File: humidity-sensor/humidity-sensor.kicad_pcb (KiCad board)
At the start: 2 copper layers, 17.8 x 142.4 mm, 9 parts, among them J1 AVR-ISP-6, J2 i2c, U1 ATtiny45-20SU

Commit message: peak-detect: add mixers humidity-sensor: fix bugs, smaller PCB
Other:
- board text added: "capacitive humidity sensor v2 lars@ibp.de"
- board text removed: "capacitive humidity sensor v1 lars@ibp.de"
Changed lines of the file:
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@@
     (effects (font (size 1 1) (thickness 0.15)))
   )
-  (gr_text "capacitive humidity \nsensor v1\nlars@ibp.de" (at 120.65 55.88) (layer F.SilkS)
+  (gr_text "capacitive humidity \nsensor v2\nlars@ibp.de" (at 120.65 55.88) (layer F.SilkS)
     (effects (font (size 1 1) (thickness 0.15)))
   )
@@
     (effects (font (size 1 1) (thickness 0.15)))
   )
-  (via (at 115.57 157.48) (size 0.8) (drill 0.4) (layers F.Cu B.Cu) (net 7))
-  (via (at 114.3 157.48) (size 0.8) (drill 0.4) (layers F.Cu B.Cu) (net 8))
   (segment (start 115.3415 42.926) (end 114.3 43.9675) (width 0.25) (layer F.Cu) (net 1))
   (segment (start 118.364 42.926) (end 115.3415 42.926) (width 0.25) (layer F.Cu) (net 1))
@@
   (segment (start 127 38.8875) (end 127.80001 39.68751) (width 0.25) (layer F.Cu) (net 2))
   (segment (start 114.3 42.3925) (end 114.3 38.8875) (width 0.25) (layer F.Cu) (net 3))
-  (segment (start 116.84 47.7775) (end 116.84 50.8) (width 0.25) (layer F.Cu) (net 11) (status 10))
-  (segment (start 116.84 50.8) (end 114.3 50.8) (width 0.25) (layer F.Cu) (net 11))
   (segment (start 116.84 29.294) (end 116.84 28.194) (width 0.25) (layer F.Cu) (net 4))
   (segment (start 120.312 32.766) (end 116.84 29.294) (width 0.25) (layer F.Cu) (net 4))
@@
   (segment (start 123.444 44.128081) (end 124.045929 44.73001) (width 0.25) (layer F.Cu) (net 4))
   (segment (start 123.444 42.926) (end 123.444 44.128081) (width 0.25) (layer F.Cu) (net 4))
-  (segment (start 114.3 50.8) (end 113.03 50.8) (width 0.25) (layer F.Cu) (net 11))
-  (segment (start 113.03 50.8) (end 113.03 53.34) (width 0.25) (layer F.Cu) (net 11))
   (segment (start 123.615 34.036) (end 124.14 34.036) (width 0.25) (layer F.Cu) (net 5))
   (segment (start 120.904 36.747) (end 123.615 34.036) (width 0.25) (layer F.Cu) (net 5))
@@
   (segment (start 123.04 36.576) (end 122.079001 37.536999) (width 0.25) (layer F.Cu) (net 6))
   (segment (start 124.14 36.576) (end 123.04 36.576) (width 0.25) (layer F.Cu) (net 6))
+  (via (at 115.57 157.48) (size 0.8) (drill 0.4) (layers F.Cu B.Cu) (net 7))
   (segment (start 118.364 39.183919) (end 118.364 40.386) (width 0.25) (layer F.Cu) (net 7))
   (segment (start 118.364 33.19) (end 118.364 39.183919) (width 0.25) (layer F.Cu) (net 7))
@@
   (segment (start 119.539001 50.640999) (end 118.11 52.07) (width 0.25) (layer F.Cu) (net 7))
   (segment (start 118.11 52.07) (end 114.3 52.07) (width 0.25) (layer F.Cu) (net 7))
+  (via (at 114.3 157.48) (size 0.8) (drill 0.4) (layers F.Cu B.Cu) (net 8))
   (segment (start 115.203506 46.115) (end 116.265 46.115) (width 0.25) (layer F.Cu) (net 8))
   (segment (start 113.49999 44.411484) (end 115.203506 46.115) (width 0.25) (layer F.Cu) (net 8))
@@
   (segment (start 116.315 34.036) (end 114.3 36.051) (width 0.25) (layer F.Cu) (net 10))
   (segment (start 116.84 34.036) (end 116.315 34.036) (width 0.25) (layer F.Cu) (net 10))
+  (segment (start 116.84 47.7775) (end 116.84 50.8) (width 0.25) (layer F.Cu) (net 11) (status 10))
+  (segment (start 116.84 50.8) (end 114.3 50.8) (width 0.25) (layer F.Cu) (net 11))
+  (segment (start 114.3 50.8) (end 113.03 50.8) (width 0.25) (layer F.Cu) (net 11))
+  (segment (start 113.03 50.8) (end 113.03 53.34) (width 0.25) (layer F.Cu) (net 11))
 )

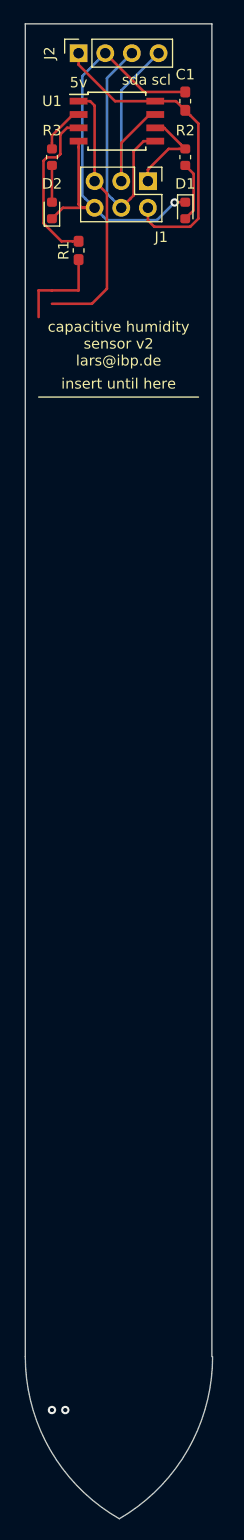
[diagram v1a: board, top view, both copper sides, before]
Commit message: Smaller is better, also fix MISO and sensing (hopefully)
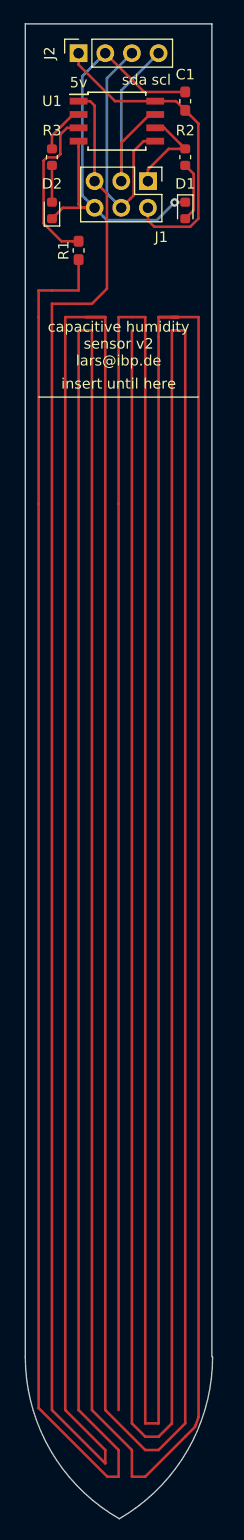
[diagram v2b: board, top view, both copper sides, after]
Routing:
- net Net-(R1-Pad1): track 9.37 -> 785.4 mm
- net /RESET: track 25.5 -> 687.5 mm, vias 1 -> 0
- net /SENSE_N: vias 1 -> 0
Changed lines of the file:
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@@
-(kicad_pcb (version 20171130) (host pcbnew "(5.1.2-1)-1")
+(kicad_pcb (version 20171130) (host pcbnew "(5.0.1-3-g963ef8bb5)")
   (general
     (thickness 1.6)
     (drawings 11)
-    (tracks 85)
+    (tracks 130)
     (zones 0)
     (modules 9)
@@
     (zone_45_only no)
     (trace_min 0.2)
+    (segment_width 0.2)
+    (edge_width 0.05)
     (via_size 0.8)
     (via_drill 0.4)
@@
     (uvia_min_size 0.2)
     (uvia_min_drill 0.1)
-    (edge_width 0.05)
-    (segment_width 0.2)
     (pcb_text_width 0.3)
     (pcb_text_size 1.5 1.5)
@@
   (segment (start 123.04 36.576) (end 122.079001 37.536999) (width 0.25) (layer F.Cu) (net 6))
   (segment (start 124.14 36.576) (end 123.04 36.576) (width 0.25) (layer F.Cu) (net 6))
-  (via (at 115.57 157.48) (size 0.8) (drill 0.4) (layers F.Cu B.Cu) (net 7))
   (segment (start 118.364 39.183919) (end 118.364 40.386) (width 0.25) (layer F.Cu) (net 7))
   (segment (start 118.364 33.19) (end 118.364 39.183919) (width 0.25) (layer F.Cu) (net 7))
@@
   (segment (start 119.539001 50.640999) (end 118.11 52.07) (width 0.25) (layer F.Cu) (net 7))
   (segment (start 118.11 52.07) (end 114.3 52.07) (width 0.25) (layer F.Cu) (net 7))
-  (via (at 114.3 157.48) (size 0.8) (drill 0.4) (layers F.Cu B.Cu) (net 8))
+  (segment (start 114.3 52.07) (end 114.3 157.48) (width 0.25) (layer F.Cu) (net 7))
+  (segment (start 114.3 157.48) (end 119.38 162.56) (width 0.25) (layer F.Cu) (net 7))
+  (segment (start 119.38 162.56) (end 119.38 161.29) (width 0.25) (layer F.Cu) (net 7))
+  (segment (start 119.38 161.29) (end 115.57 157.48) (width 0.25) (layer F.Cu) (net 7))
+  (segment (start 115.57 157.48) (end 115.57 53.34) (width 0.25) (layer F.Cu) (net 7))
+  (segment (start 115.57 53.34) (end 119.38 53.34) (width 0.25) (layer F.Cu) (net 7))
+  (segment (start 119.38 53.34) (end 117.47641 53.34) (width 0.25) (layer F.Cu) (net 7))
+  (segment (start 124.46 161.29) (end 127 158.75) (width 0.25) (layer F.Cu) (net 7))
+  (segment (start 127 158.75) (end 127 54.61) (width 0.25) (layer F.Cu) (net 7))
+  (segment (start 123.19 161.29) (end 124.46 161.29) (width 0.25) (layer F.Cu) (net 7))
+  (segment (start 119.38 157.48) (end 123.19 161.29) (width 0.25) (layer F.Cu) (net 7))
+  (segment (start 119.38 53.34) (end 119.38 157.48) (width 0.25) (layer F.Cu) (net 7))
+  (segment (start 127 54.61) (end 125.73 54.61) (width 0.25) (layer F.Cu) (net 7))
+  (segment (start 125.73 54.61) (end 125.73 158.75) (width 0.25) (layer F.Cu) (net 7))
+  (segment (start 125.73 158.75) (end 124.46 160.02) (width 0.25) (layer F.Cu) (net 7))
+  (segment (start 124.46 160.02) (end 123.19 160.02) (width 0.25) (layer F.Cu) (net 7))
+  (segment (start 123.19 160.02) (end 121.92 158.75) (width 0.25) (layer F.Cu) (net 7))
+  (segment (start 121.92 158.75) (end 121.92 54.61) (width 0.25) (layer F.Cu) (net 7))
   (segment (start 115.203506 46.115) (end 116.265 46.115) (width 0.25) (layer F.Cu) (net 8))
   (segment (start 113.49999 44.411484) (end 115.203506 46.115) (width 0.25) (layer F.Cu) (net 8))
@@
   (segment (start 114.3 50.8) (end 113.03 50.8) (width 0.25) (layer F.Cu) (net 11))
   (segment (start 113.03 50.8) (end 113.03 53.34) (width 0.25) (layer F.Cu) (net 11))
+  (segment (start 113.03 53.34) (end 113.03 71.12) (width 0.25) (layer F.Cu) (net 11))
+  (segment (start 113.03 157.283002) (end 119.576998 163.83) (width 0.25) (layer F.Cu) (net 11))
+  (segment (start 113.03 71.12) (end 113.03 157.283002) (width 0.25) (layer F.Cu) (net 11))
+  (segment (start 119.576998 163.83) (end 120.65 163.83) (width 0.25) (layer F.Cu) (net 11))
+  (segment (start 120.65 163.83) (end 120.65 161.29) (width 0.25) (layer F.Cu) (net 11))
+  (segment (start 120.65 161.29) (end 116.84 157.48) (width 0.25) (layer F.Cu) (net 11))
+  (segment (start 116.84 157.48) (end 116.84 54.61) (width 0.25) (layer F.Cu) (net 11))
+  (segment (start 116.84 54.61) (end 118.11 54.61) (width 0.25) (layer F.Cu) (net 11))
+  (segment (start 118.11 54.61) (end 118.11 157.48) (width 0.25) (layer F.Cu) (net 11))
+  (segment (start 118.11 157.48) (end 121.92 161.29) (width 0.25) (layer F.Cu) (net 11))
+  (segment (start 121.92 161.29) (end 121.92 163.83) (width 0.25) (layer F.Cu) (net 11))
+  (segment (start 121.92 163.83) (end 123.19 163.83) (width 0.25) (layer F.Cu) (net 11))
+  (segment (start 123.19 163.83) (end 127 160.02) (width 0.25) (layer F.Cu) (net 11))
+  (segment (start 128.009948 158.890228) (end 128.27 158.137132) (width 0.25) (layer F.Cu) (net 11))
+  (segment (start 127.909676 159.110324) (end 128.009948 158.890228) (width 0.25) (layer F.Cu) (net 11))
+  (segment (start 127 160.02) (end 127.909676 159.110324) (width 0.25) (layer F.Cu) (net 11))
+  (segment (start 128.27 158.137132) (end 128.27 53.34) (width 0.25) (layer F.Cu) (net 11))
+  (segment (start 128.27 53.34) (end 125.73 53.34) (width 0.25) (layer F.Cu) (net 11))
+  (segment (start 125.73 53.34) (end 126.36641 53.34) (width 0.25) (layer F.Cu) (net 11))
+  (segment (start 125.73 53.34) (end 124.46 53.34) (width 0.25) (layer F.Cu) (net 11))
+  (segment (start 124.46 53.34) (end 126.36359 53.34) (width 0.25) (layer F.Cu) (net 11))
+  (segment (start 124.46 55.24359) (end 124.46 158.75) (width 0.25) (layer F.Cu) (net 11))
+  (segment (start 124.46 158.75) (end 123.19 158.75) (width 0.25) (layer F.Cu) (net 11))
+  (segment (start 123.19 158.75) (end 123.19 53.34) (width 0.25) (layer F.Cu) (net 11))
+  (segment (start 124.46 55.24359) (end 124.46 53.34) (width 0.25) (layer F.Cu) (net 11))
+  (segment (start 123.19 53.34) (end 121.92 53.34) (width 0.25) (layer F.Cu) (net 11))
+  (segment (start 121.92 53.34) (end 120.65 53.34) (width 0.25) (layer F.Cu) (net 11))
+  (segment (start 120.65 53.34) (end 120.65 71.12) (width 0.25) (layer F.Cu) (net 11))
+  (segment (start 120.65 71.12) (end 120.65 157.48) (width 0.25) (layer F.Cu) (net 11))
 )

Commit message: Add capsensor, humidity sensor p3, garduino with avr
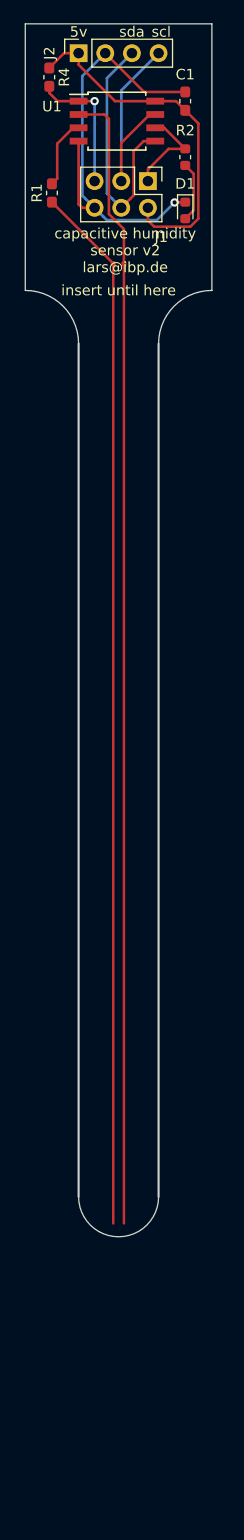
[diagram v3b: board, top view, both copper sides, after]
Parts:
- removed D2: LED, LED_SMD:LED_0603_1608Metric
- removed R3: 1k, Resistor_SMD:R_0603_1608Metric
- added C2: capsensor, lci-kicad:capsensor, F.Cu at (120.7, 48.3)
- added R4: 10k, Resistor_SMD:R_0603_1608Metric_Pad1.05x0.95mm_HandSolder, F.Cu at (114.0, 30.5)
- moved R1 6.04 mm to (114.3, 41.5)
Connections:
- net /SENSE_N renamed Net-(R1-Pad2)
- U1 pad 2: /PB3 -> Net-(C2-Pad2)
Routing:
- net Net-(C2-Pad1): track 785.4 -> 8.29 mm
- net /RESET: track 687.5 -> 12.9 mm, vias 0 -> 1
- net Net-(C2-Pad2): track 0.00 -> 18.0 mm
- net Net-(R1-Pad2): track 15.7 -> 6.69 mm
- net /PB3: track 4.64 -> 0.00 mm
- net GND: track 47.3 -> 42.8 mm
- net Net-(D2-Pad2): track 3.50 -> 0.00 mm
- net +5V: track 30.5 -> 33.9 mm
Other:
- board size 17.8 x 142.4 mm -> 17.8 x 115.6 mm
